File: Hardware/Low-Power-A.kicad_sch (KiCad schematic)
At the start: 27 parts, among them J1 USB_A, J2 01x02, Q1 BC557, Q2 BC547, Q3 BC557, Q4 BC547, Q5 BC547, U1 Arduino_Pro_Micro, U2 VS1838B

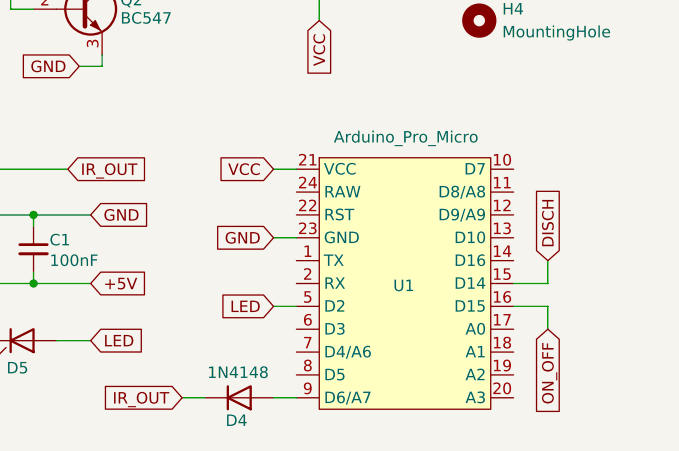
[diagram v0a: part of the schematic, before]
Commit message: Adding Low-Power-B version schematics & PCB
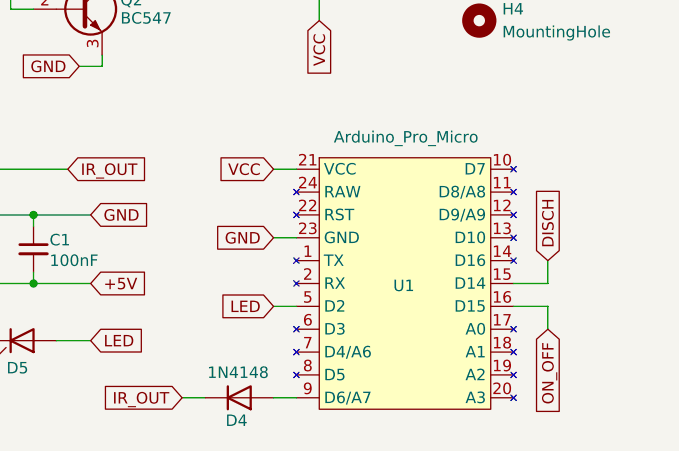
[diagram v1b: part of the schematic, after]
